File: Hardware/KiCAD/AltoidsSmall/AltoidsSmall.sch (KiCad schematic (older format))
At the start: 8 parts, among them U1 SC662K-3.3V, U4 USB_B_micro, U6 SC662K-3.3V

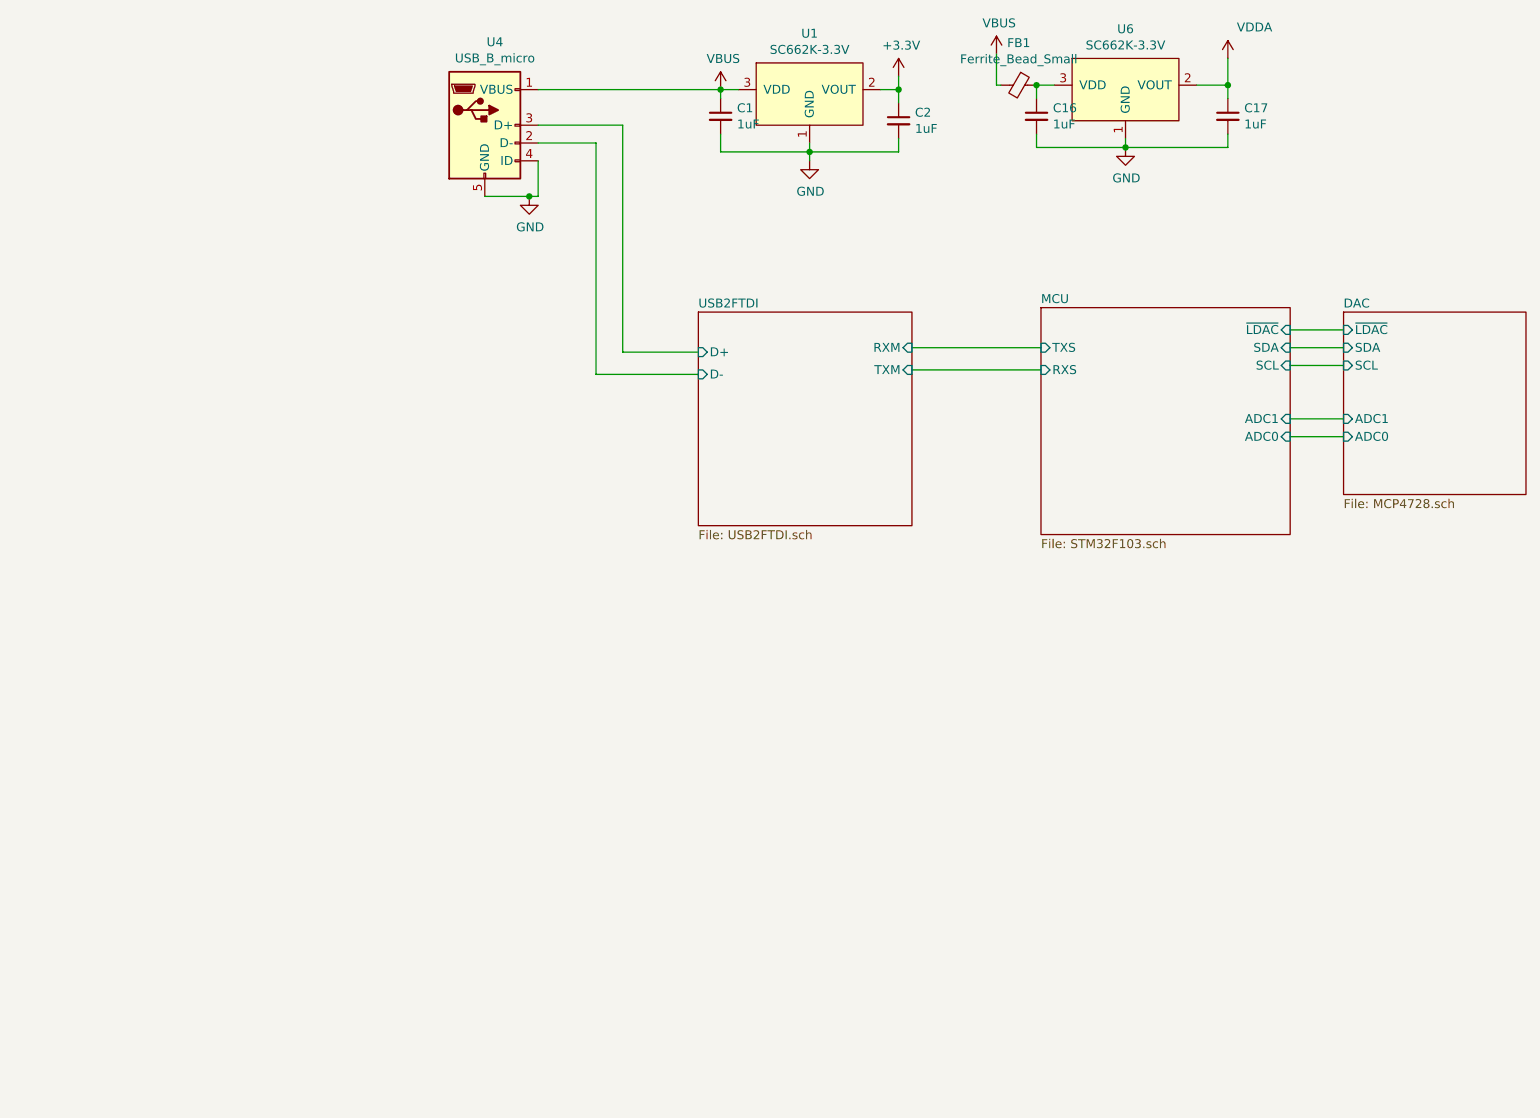
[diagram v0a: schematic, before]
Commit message: Added labels to pins, Added part numbers
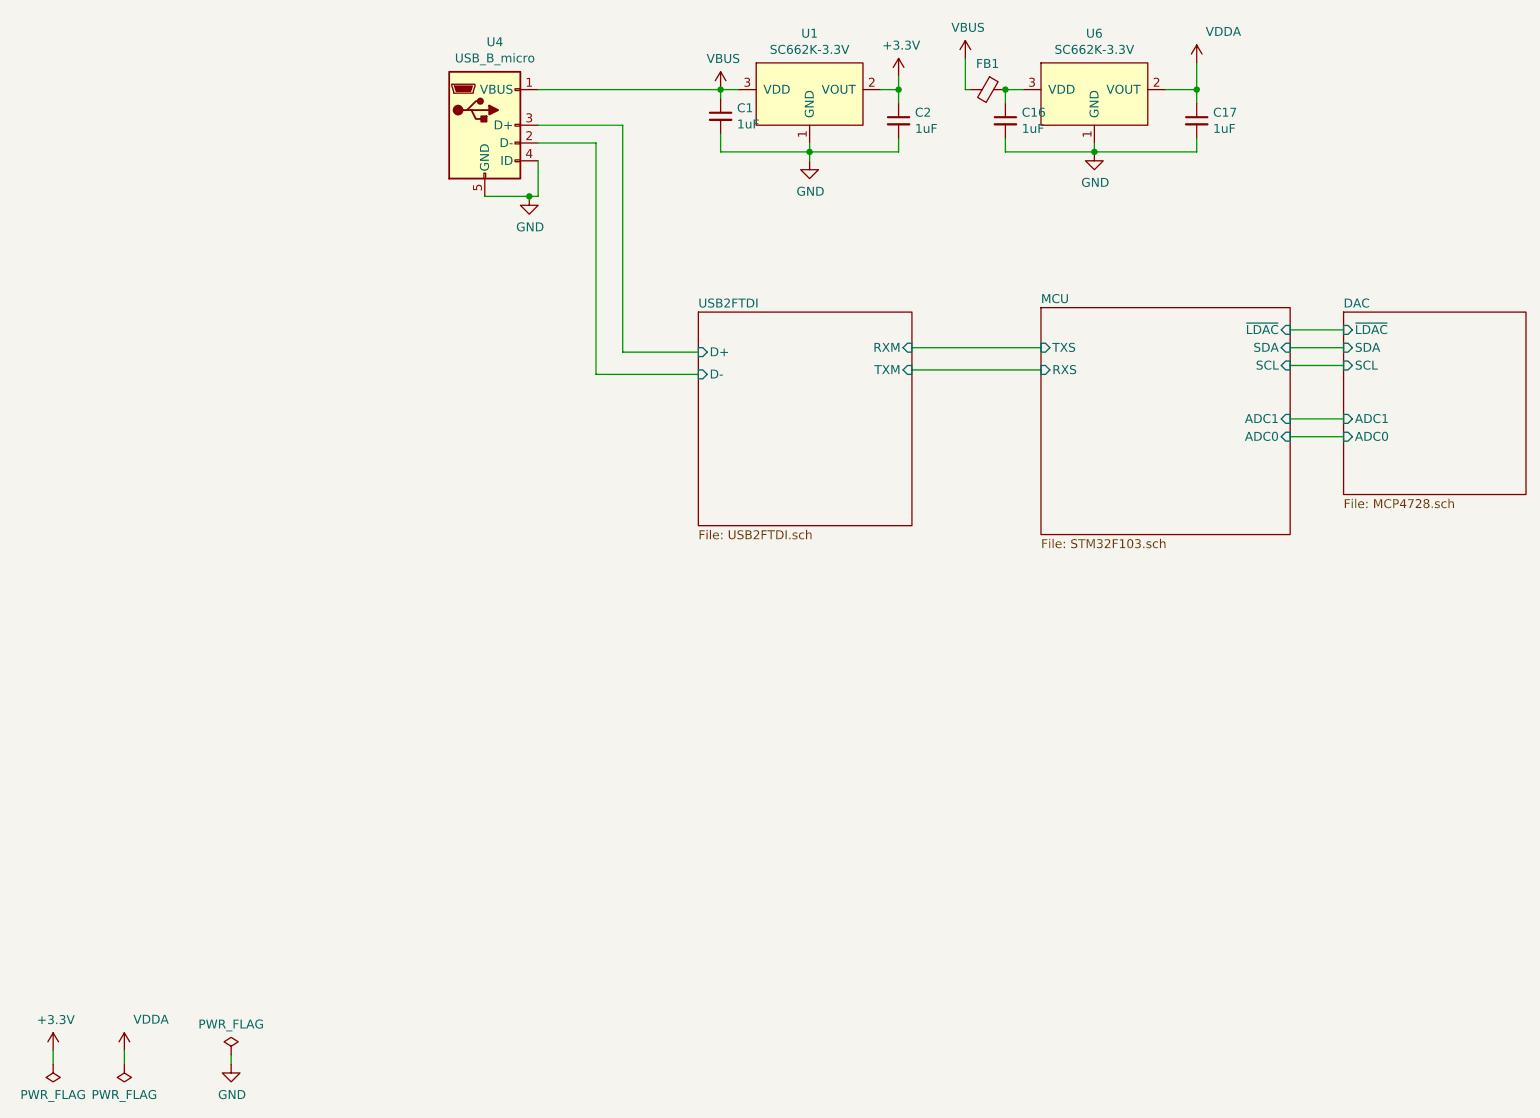
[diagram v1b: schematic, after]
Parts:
- C1, C16, C17, C2: Digikey (none) -> 1276-6524-1-ND
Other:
- moved on the sheet: C16, C17, FB1, U6
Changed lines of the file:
@@
 F 2 "Capacitor_SMD:C_0603_1608Metric_Pad1.05x0.95mm_HandSolder" H 5600 2125 50  0001 C CNN
 F 3 "~" H 5600 2125 50  0001 C CNN
+F 4 "1276-6524-1-ND" H 5600 2125 50  0001 C CNN "Digikey"
 	1    5600 2125
 	1    0    0    -1
@@
 F 2 "Capacitor_SMD:C_0603_1608Metric_Pad1.05x0.95mm_HandSolder" H 4600 2100 50  0001 C CNN
 F 3 "~" H 4600 2100 50  0001 C CNN
+F 4 "1276-6524-1-ND" H 4600 2100 50  0001 C CNN "Digikey"
 	1    4600 2100
 	1    0    0    -1
@@
 L power:VDDA #PWR?
 U 1 1 5FF491A6
-P 7450 1775
+P 7275 1800
 AR Path="/5FF2DABE/5FF491A6" Ref="#PWR?"  Part="1"
 AR Path="/5FF491A6" Ref="#PWR03"  Part="1"
-F 0 "#PWR03" H 7450 1625 50  0001 C CNN
-F 1 "VDDA" H 7600 1950 50  0000 C CNN
-F 2 "" H 7450 1775 50  0001 C CNN
-F 3 "" H 7450 1775 50  0001 C CNN
-	1    7450 1775
+F 0 "#PWR03" H 7275 1650 50  0001 C CNN
+F 1 "VDDA" H 7425 1975 50  0000 C CNN
+F 2 "" H 7275 1800 50  0001 C CNN
+F 3 "" H 7275 1800 50  0001 C CNN
+	1    7275 1800
 	1    0    0    -1
 $EndComp
@@
 L AltoidsSmall:SC662K-3.3V U6
 U 1 1 6004B04E
-P 6875 1925
-F 0 "U6" H 6875 2240 50  0000 C CNN
-F 1 "SC662K-3.3V" H 6875 2149 50  0000 C CNN
-F 2 "Package_TO_SOT_SMD:SOT-23" H 6875 1925 50  0001 C CNN
-F 3 "" H 6875 1925 50  0001 C CNN
-	1    6875 1925
+P 6700 1950
+F 0 "U6" H 6700 2265 50  0000 C CNN
+F 1 "SC662K-3.3V" H 6700 2174 50  0000 C CNN
+F 2 "Package_TO_SOT_SMD:SOT-23" H 6700 1950 50  0001 C CNN
+F 3 "" H 6700 1950 50  0001 C CNN
+	1    6700 1950
 	1    0    0    -1
 $EndComp
@@
 L power:VBUS #PWR0104
 U 1 1 600D02ED
-P 6150 1750
-F 0 "#PWR0104" H 6150 1600 50  0001 C CNN
-F 1 "VBUS" H 6165 1923 50  0000 C CNN
-F 2 "" H 6150 1750 50  0001 C CNN
-F 3 "" H 6150 1750 50  0001 C CNN
-	1    6150 1750
-	1    0    0    -1
-$EndComp
-Wire Wire Line
-	6150 1750 6150 1925
-Wire Wire Line
-	6150 1925 6175 1925
-Wire Wire Line
-	7450 1775 7450 1925
-Wire Wire Line
-	7275 1925 7450 1925
+P 5975 1775
+F 0 "#PWR0104" H 5975 1625 50  0001 C CNN
+F 1 "VBUS" H 5990 1948 50  0000 C CNN
+F 2 "" H 5975 1775 50  0001 C CNN
+F 3 "" H 5975 1775 50  0001 C CNN
+	1    5975 1775
+	1    0    0    -1
+$EndComp
+Wire Wire Line
+	5975 1775 5975 1950
+Wire Wire Line
+	5975 1950 6000 1950
+Wire Wire Line
+	7275 1800 7275 1950
+Wire Wire Line
+	7100 1950 7275 1950
 $Comp
 L power:GND #PWR0105
 U 1 1 600D1E2D
-P 6875 2275
-F 0 "#PWR0105" H 6875 2025 50  0001 C CNN
-F 1 "GND" H 6880 2102 50  0000 C CNN
-F 2 "" H 6875 2275 50  0001 C CNN
-F 3 "" H 6875 2275 50  0001 C CNN
-	1    6875 2275
-	1    0    0    -1
-$EndComp
-Wire Wire Line
-	6875 2225 6875 2275
+P 6700 2300
+F 0 "#PWR0105" H 6700 2050 50  0001 C CNN
+F 1 "GND" H 6705 2127 50  0000 C CNN
+F 2 "" H 6700 2300 50  0001 C CNN
+F 3 "" H 6700 2300 50  0001 C CNN
+	1    6700 2300
+	1    0    0    -1
+$EndComp
+Wire Wire Line
+	6700 2250 6700 2300
 $Comp
 L Device:C_Small C16
 U 1 1 600E49EE
-P 6375 2100
-F 0 "C16" H 6467 2146 50  0000 L CNN
-F 1 "1uF" H 6467 2055 50  0000 L CNN
-F 2 "Capacitor_SMD:C_0603_1608Metric_Pad1.05x0.95mm_HandSolder" H 6375 2100 50  0001 C CNN
-F 3 "~" H 6375 2100 50  0001 C CNN
-	1    6375 2100
+P 6200 2125
+F 0 "C16" H 6292 2171 50  0000 L CNN
+F 1 "1uF" H 6292 2080 50  0000 L CNN
+F 2 "Capacitor_SMD:C_0603_1608Metric_Pad1.05x0.95mm_HandSolder" H 6200 2125 50  0001 C CNN
+F 3 "~" H 6200 2125 50  0001 C CNN
+F 4 "1276-6524-1-ND" H 6200 2125 50  0001 C CNN "Digikey"
+	1    6200 2125
 	1    0    0    -1
 $EndComp
@@
 L Device:C_Small C17
 U 1 1 600E5351
-P 7450 2100
-F 0 "C17" H 7542 2146 50  0000 L CNN
-F 1 "1uF" H 7542 2055 50  0000 L CNN
-F 2 "Capacitor_SMD:C_0603_1608Metric_Pad1.05x0.95mm_HandSolder" H 7450 2100 50  0001 C CNN
-F 3 "~" H 7450 2100 50  0001 C CNN
-	1    7450 2100
-	1    0    0    -1
-$EndComp
-Wire Wire Line
-	6375 2275 6875 2275
-Connection ~ 6875 2275
-Wire Wire Line
-	7450 1925 7450 2000
-Wire Wire Line
-	7450 2275 6875 2275
-Wire Wire Line
-	7450 2200 7450 2275
-Connection ~ 7450 1925
-Wire Wire Line
-	6475 1925 6375 1925
-Wire Wire Line
-	6375 1925 6375 2000
-Wire Wire Line
-	6375 2200 6375 2275
+P 7275 2125
+F 0 "C17" H 7367 2171 50  0000 L CNN
+F 1 "1uF" H 7367 2080 50  0000 L CNN
+F 2 "Capacitor_SMD:C_0603_1608Metric_Pad1.05x0.95mm_HandSolder" H 7275 2125 50  0001 C CNN
+F 3 "~" H 7275 2125 50  0001 C CNN
+F 4 "1276-6524-1-ND" H 7275 2125 50  0001 C CNN "Digikey"
+	1    7275 2125
+	1    0    0    -1
+$EndComp
+Wire Wire Line
+	6200 2300 6700 2300
+Connection ~ 6700 2300
+Wire Wire Line
+	7275 1950 7275 2025
+Wire Wire Line
+	7275 2300 6700 2300
+Wire Wire Line
+	7275 2225 7275 2300
+Connection ~ 7275 1950
+Wire Wire Line
+	6300 1950 6200 1950
+Wire Wire Line
+	6200 1950 6200 2025
+Wire Wire Line
+	6200 2225 6200 2300
 $Comp
 L Device:Ferrite_Bead_Small FB1
 U 1 1 600F614B
-P 6275 1925
-F 0 "FB1" V 6038 1925 50  0000 C CNN
-F 1 "Ferrite_Bead_Small" V 6129 1925 50  0000 C CNN
-F 2 "Capacitor_SMD:C_0805_2012Metric" V 6205 1925 50  0001 C CNN
-F 3 "~" H 6275 1925 50  0001 C CNN
-F 4 "490-5229-1-ND" V 6275 1925 50  0001 C CNN "Digikey"
-	1    6275 1925
+P 6100 1950
+F 0 "FB1" V 5955 1950 50  0000 C CNN
+F 1 "Ferrite_Bead_Small" V 5954 1950 50  0001 C CNN
+F 2 "Capacitor_SMD:C_0805_2012Metric" V 6030 1950 50  0001 C CNN
+F 3 "~" H 6100 1950 50  0001 C CNN
+F 4 "490-5229-1-ND" V 6100 1950 50  0001 C CNN "Digikey"
+	1    6100 1950
 	0    1    1    0
 $EndComp
-Connection ~ 6375 1925
+Connection ~ 6200 1950
+$Comp
+L power:PWR_FLAG #FLG0101
+U 1 1 6013D1B8
+P 850 7425
+F 0 "#FLG0101" H 850 7500 50  0001 C CNN
+F 1 "PWR_FLAG" H 850 7598 50  0000 C CNN
+F 2 "" H 850 7425 50  0001 C CNN
+F 3 "~" H 850 7425 50  0001 C CNN
+	1    850  7425
+	-1   0    0    1
+$EndComp
+$Comp
+L power:PWR_FLAG #FLG0102
+U 1 1 6013DECB
+P 1250 7425
+F 0 "#FLG0102" H 1250 7500 50  0001 C CNN
+F 1 "PWR_FLAG" H 1250 7598 50  0000 C CNN
+F 2 "" H 1250 7425 50  0001 C CNN
+F 3 "~" H 1250 7425 50  0001 C CNN
+	1    1250 7425
+	-1   0    0    1
+$EndComp
+$Comp
+L AltoidsSmall:+3.3V #PWR0110
+U 1 1 601421D4
+P 850 7350
+F 0 "#PWR0110" H 850 7200 50  0001 C CNN
+F 1 "+3.3V" H 865 7523 50  0000 C CNN
+F 2 "" H 850 7350 50  0001 C CNN
+F 3 "" H 850 7350 50  0001 C CNN
+	1    850  7350
+	1    0    0    -1
+$EndComp
+$Comp
+L power:VDDA #PWR?
+U 1 1 60143A35
+P 1250 7350
+AR Path="/5FF2DABE/60143A35" Ref="#PWR?"  Part="1"
+AR Path="/60143A35" Ref="#PWR0111"  Part="1"
+F 0 "#PWR0111" H 1250 7200 50  0001 C CNN
+F 1 "VDDA" H 1400 7525 50  0000 C CNN
+F 2 "" H 1250 7350 50  0001 C CNN
+F 3 "" H 1250 7350 50  0001 C CNN
+	1    1250 7350
+	1    0    0    -1
+$EndComp
+Wire Wire Line
+	850  7350 850  7425
+Wire Wire Line
+	1250 7350 1250 7425
+$Comp
+L power:PWR_FLAG #FLG0103
+U 1 1 6014A5D2
+P 1850 7375
+F 0 "#FLG0103" H 1850 7450 50  0001 C CNN
+F 1 "PWR_FLAG" H 1850 7548 50  0000 C CNN
+F 2 "" H 1850 7375 50  0001 C CNN
+F 3 "~" H 1850 7375 50  0001 C CNN
+	1    1850 7375
+	1    0    0    -1
+$EndComp
+$Comp
+L power:GND #PWR0112
+U 1 1 6014B19E
+P 1850 7425
+F 0 "#PWR0112" H 1850 7175 50  0001 C CNN
+F 1 "GND" H 1855 7252 50  0000 C CNN
+F 2 "" H 1850 7425 50  0001 C CNN
+F 3 "" H 1850 7425 50  0001 C CNN
+	1    1850 7425
+	1    0    0    -1
+$EndComp
+Wire Wire Line
+	1850 7375 1850 7425
 $EndSCHEMATC
